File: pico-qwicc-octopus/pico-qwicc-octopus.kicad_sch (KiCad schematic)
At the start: 21 parts, among them U1 RP2040

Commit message: Trying to get just the basics working.
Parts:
- removed D1, D2, D3, D4, D6, D7, D8: LED, LED_SMD:LED_0805_2012Metric, symbol Device:LED
- removed D5: LED, symbol Device:LED
- removed R10, R11, R12, R5, R6, R7, R8, R9: 220, Resistor_SMD:R_0805_2012Metric, symbol Device:R
- removed U1: RP2040, Package_DFN_QFN:QFN-56-1EP_7x7mm_P0.4mm_EP3.2x3.2mm, symbol MCU_RaspberryPi:RP2040
- added J1: B3B-XH-A, CONN_B3B-XH-A_JST, symbol Ivan Hawkes:B3B-XH-A
- added J2: BM04B-SRSS-TB, CONN4_BM04B-SRSS_JST, symbol Ivan Hawkes:BM04B-SRSS-TB
- added U1: Raspberry Pi Pico, Footprint, symbol Ivan Hawkes:Raspberry_Pi_Pico
- R3, R4: value 250 -> 100
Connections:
- net GND: now also J1.2, J2.1, U1.38 (GND)
- net TX: now reaches R1.1
- net TX: now also U1.1 (GPIO0)
- net RX: now reaches R2.1
- net RX: now also U1.2 (GPIO1)
- net SDA: now reaches R3.1
- net SDA: now also U1.6 (GPIO4)
- net SCL: now reaches R4.1
- net SCL: now also U1.7 (GPIO5)
- net at R2.2: now also J1.3
- net at R1.2: now also J1.1
- net +3.3V: no longer names the net of R4.2
- net +3.3V: now also J2.4; no longer R3.2
- new net: J2.3, R3.2
- new net +3V3: J2.2, U1.36 (3V3)
- no-connect marks 24 -> 29
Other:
- moved on the sheet: R1, R2

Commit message: Trying to get a good working symbol for the RPi Pico board.
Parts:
- removed R3, R4: 100, Resistor_SMD:R_0805_2012Metric, symbol Device:R
- removed U1: Raspberry Pi Pico, Footprint, symbol Ivan Hawkes:Raspberry_Pi_Pico
- added U1: Pico, RPi_Pico:RPi_Pico_SMD_TH, symbol Ivan Hawkes:Pico
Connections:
- net GND: now also U1.42 (GND)
- net RX: now also U1.1 (GPIO0)
- net SCL: now also J2.4, U1.7 (GPIO5)
- net SDA: now also J2.3, U1.6 (GPIO4)
- net TX: now also U1.2 (GPIO1)
- net +3V3: no longer names the net of J2.2
- no-connect marks 29 -> 39
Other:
- moved on the sheet: J1, J2, R1, R2

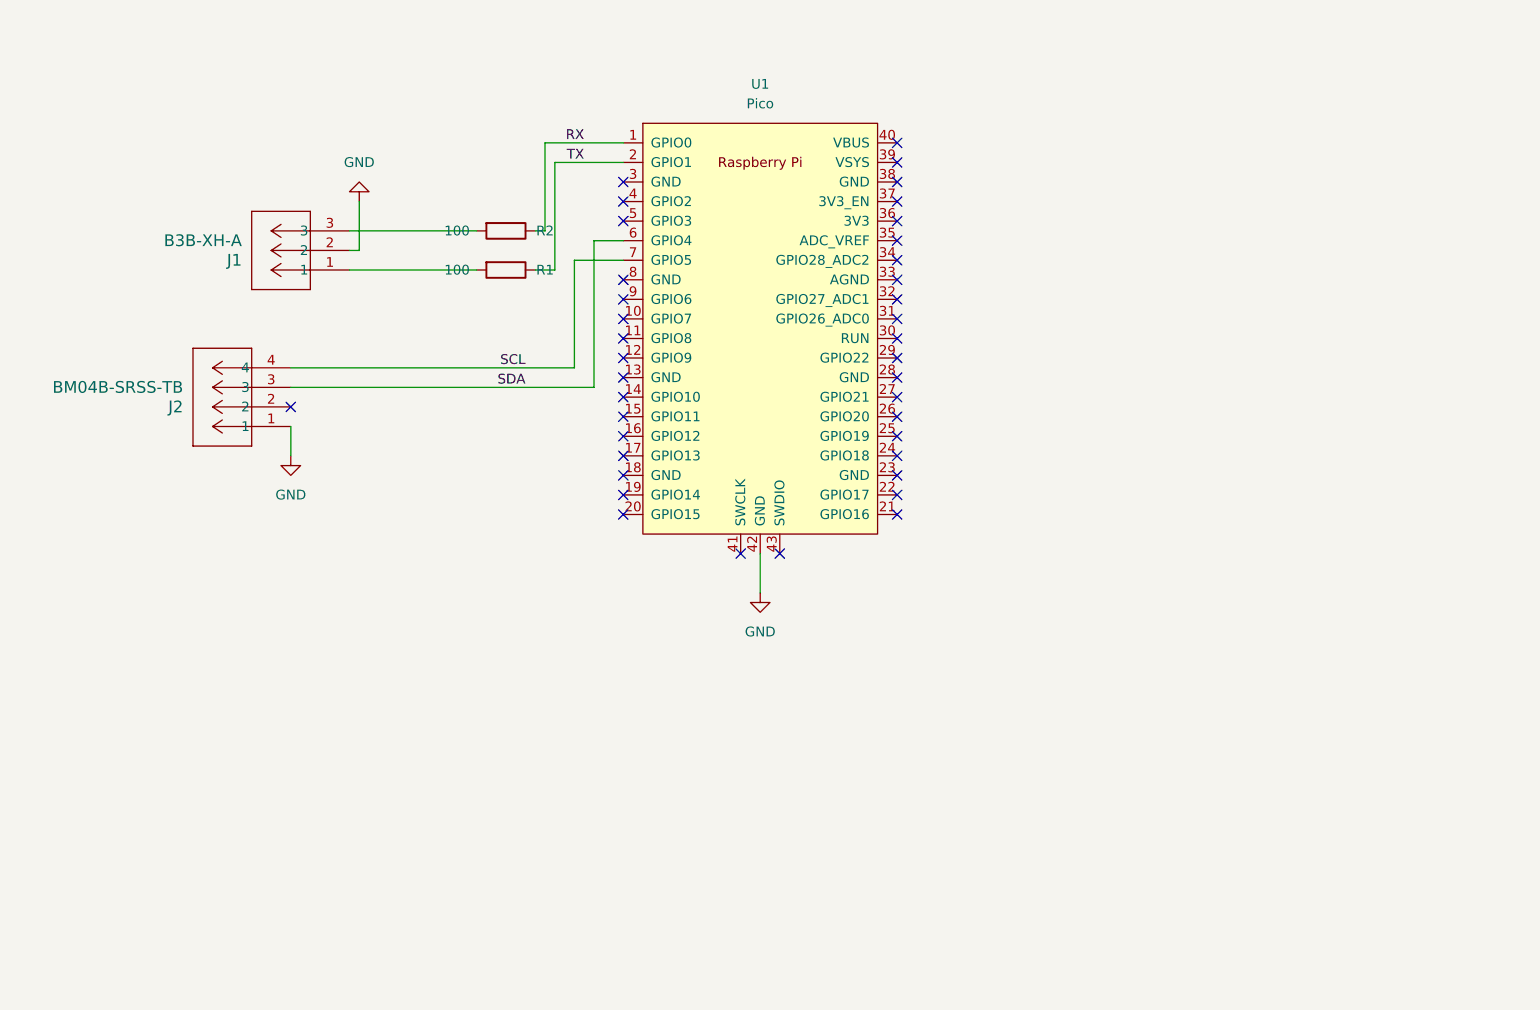
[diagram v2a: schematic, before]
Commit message: Finally getting the hang of routing. Found out how to stop warnings on ERC tests.
Considering having the board with only a couple of separate I2C connections. It seems they work better when routed through instead of a star configuration.
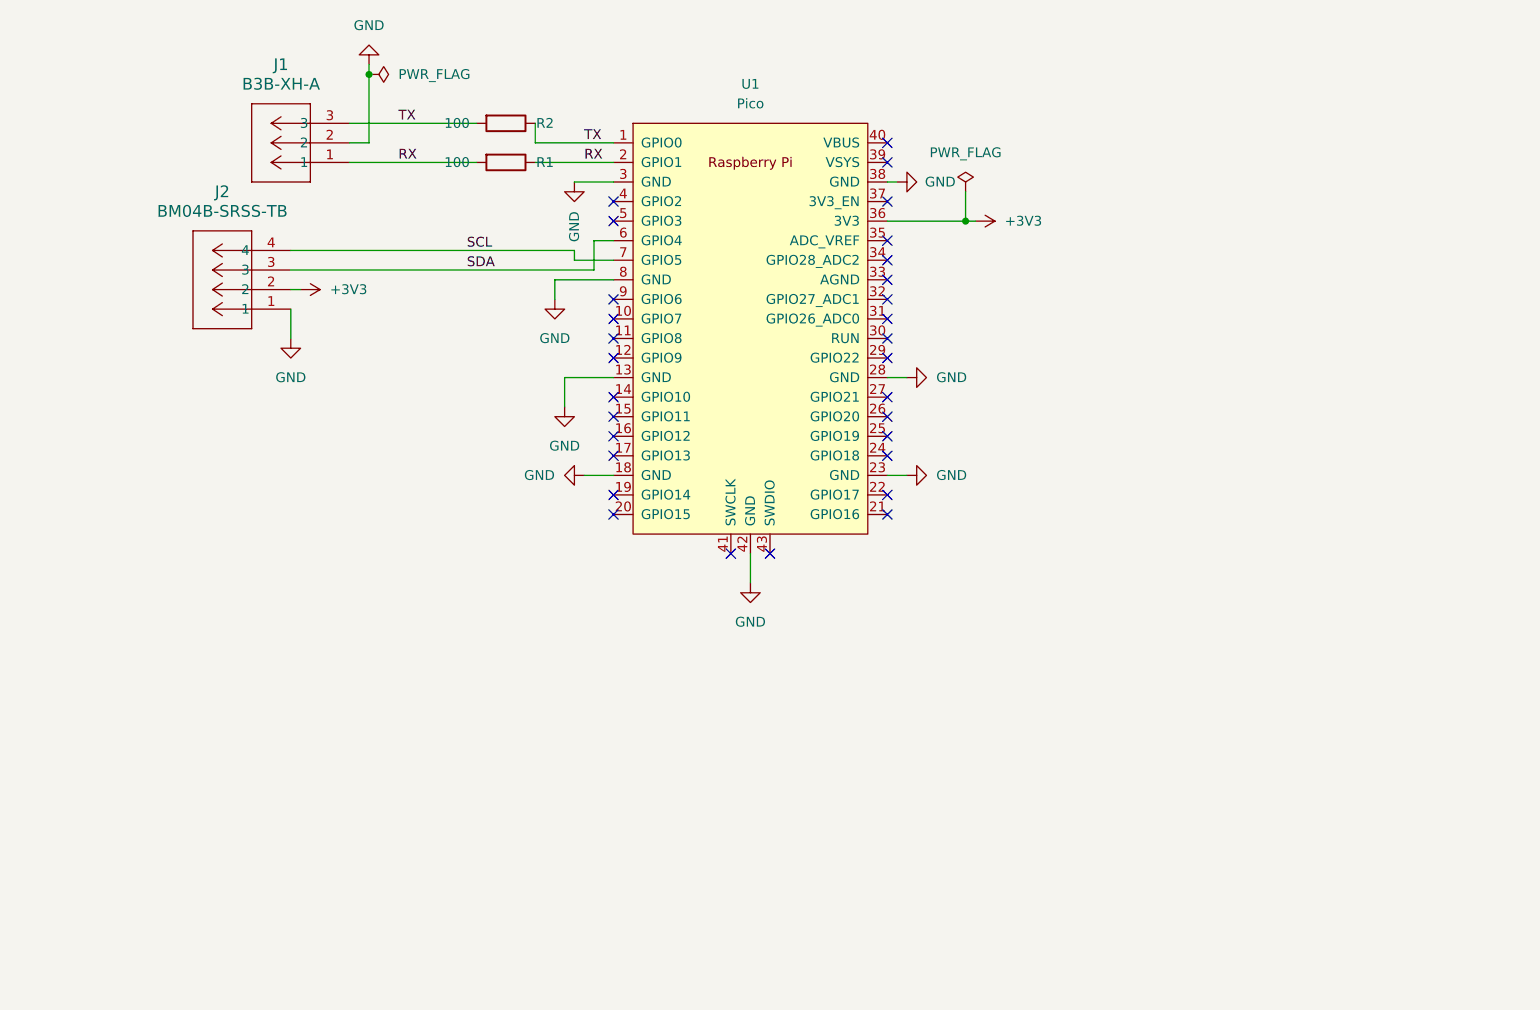
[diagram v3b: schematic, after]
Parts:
- removed J1: B3B-XH-A, CONN_B3B-XH-A_JST, symbol Ivan Hawkes:B3B-XH-A
- removed J2: BM04B-SRSS-TB, CONN4_BM04B-SRSS_JST, symbol Ivan Hawkes:BM04B-SRSS-TB
- removed U1: Pico, RPi_Pico:RPi_Pico_SMD_TH, symbol Ivan Hawkes:Pico
- added J1: B3B-XH-A, 00_Connectors:JST-B3B-XH-A, symbol 00_Connectors:B3B-XH-A
- added J2: BM04B-SRSS-TB, 00_Connectors:JST-BM04B-SRSS, symbol 00_Connectors:BM04B-SRSS-TB
- added U1: Pico, 00_General:RPi-Pico-SMD-TH, symbol 00_General:Pico
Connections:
- net GND: now also J1.2, J2.1, U1.13 (GND), U1.18 (GND), U1.23 (GND), U1.28 (GND), U1.3 (GND), U1.38 (GND), U1.42 (GND), U1.8 (GND)
- net RX: now also R1.1, R1.2, J1.1, U1.2 (GPIO1); no longer R2.1
- net SCL: now also J2.4, U1.7 (GPIO5)
- net SDA: now also J2.3, U1.6 (GPIO4)
- net TX: now also R2.1, R2.2, J1.3, U1.1 (GPIO0); no longer R1.1
- new net +3V3: J2.2, U1.36 (3V3)
- no-connect marks 39 -> 30
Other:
- moved on the sheet: R1, R2
